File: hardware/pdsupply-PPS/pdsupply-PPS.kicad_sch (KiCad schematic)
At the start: 73 parts, among them IC1 LTM8083EY#PBF, IC2 FPF2895UCX, J1 USB4505-03-0-A_REVA, J2 USB4505-03-0-A_REVA, J3 Screw_Terminal_01x02, U1 FUSB307BMPX, U2 ADUM3160, U3 ACS71240KEXBLT-050U5, U4 STM32L432KCUx

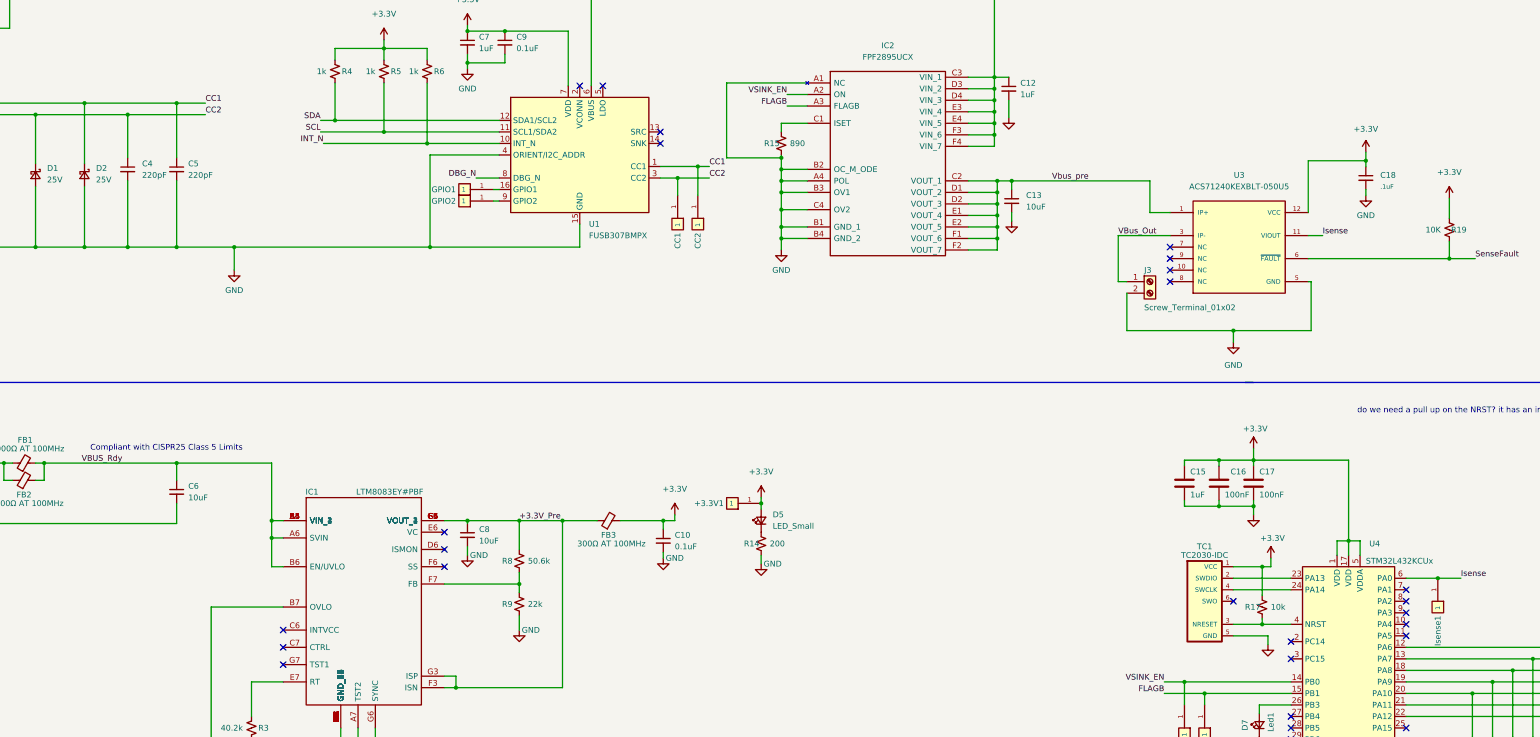
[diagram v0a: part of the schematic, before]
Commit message: changed Pin A1 on FPF2895 to be connected to GND
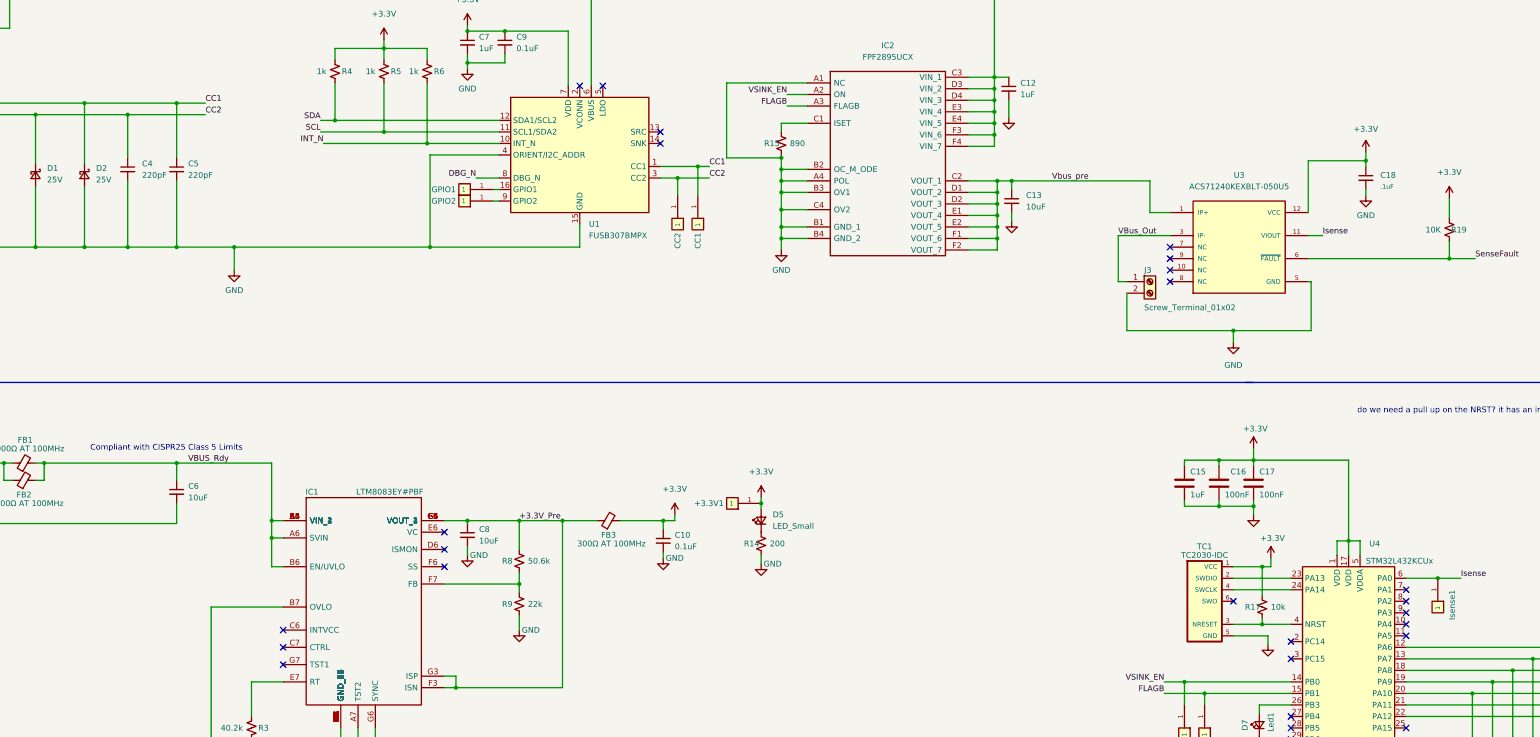
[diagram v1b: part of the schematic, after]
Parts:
- renumbered CC2 to CC1, CC1 to CC2
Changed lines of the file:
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@@
     (effects (font (size 1.27 1.27)) (justify left bottom))
   )
-  (label "VBUS_Rdy" (at 67.945 127 0)
+  (label "VBUS_Rdy" (at 91.44 127 0)
     (effects (font (size 1.27 1.27)) (justify left bottom))
   )
@@
   (symbol (lib_name "RCU-0C_1") (lib_id "RCU-0C:RCU-0C") (at 199.39 78.105 270) (unit 1)
     (in_bom yes) (on_board yes)
-    (property "Reference" "CC1" (id 0) (at 199.39 76.2 0)
+    (property "Reference" "CC2" (id 0) (at 199.39 76.2 0)
       (effects (font (size 1.27 1.27)) (justify left))
     )
@@
   (symbol (lib_name "RCU-0C_1") (lib_id "RCU-0C:RCU-0C") (at 203.835 78.105 270) (unit 1)
     (in_bom yes) (on_board yes)
-    (property "Reference" "CC2" (id 0) (at 203.835 76.2 0)
+    (property "Reference" "CC1" (id 0) (at 203.835 76.2 0)
       (effects (font (size 1.27 1.27)) (justify left))
     )
@@
   (symbol (lib_name "RCU-0C_1") (lib_id "RCU-0C:RCU-0C") (at 367.03 162.56 270) (unit 1)
     (in_bom yes) (on_board yes)
-    (property "Reference" "Isense1" (id 0) (at 367.03 160.655 0)
+    (property "Reference" "Isense1" (id 0) (at 370.205 154.94 0)
       (effects (font (size 1.27 1.27)) (justify left))
     )
@@
       (reference "C18") (unit 1) (value ".1uF") (footprint "Capacitor_SMD:C_0603_1608Metric")
     )
+    (path "/8aae3a86-de62-4041-9db6-c32f65e87d6d"
+      (reference "CC1") (unit 1) (value "RCU-0C") (footprint "RCU-0C:TP+195X110")
+    )
     (path "/28ec1f29-4986-4a9a-a39a-5d540d191da2"
-      (reference "CC1") (unit 1) (value "RCU-0C") (footprint "RCU-0C:TP+195X110")
-    )
-    (path "/8aae3a86-de62-4041-9db6-c32f65e87d6d"
       (reference "CC2") (unit 1) (value "RCU-0C") (footprint "RCU-0C:TP+195X110")
     )

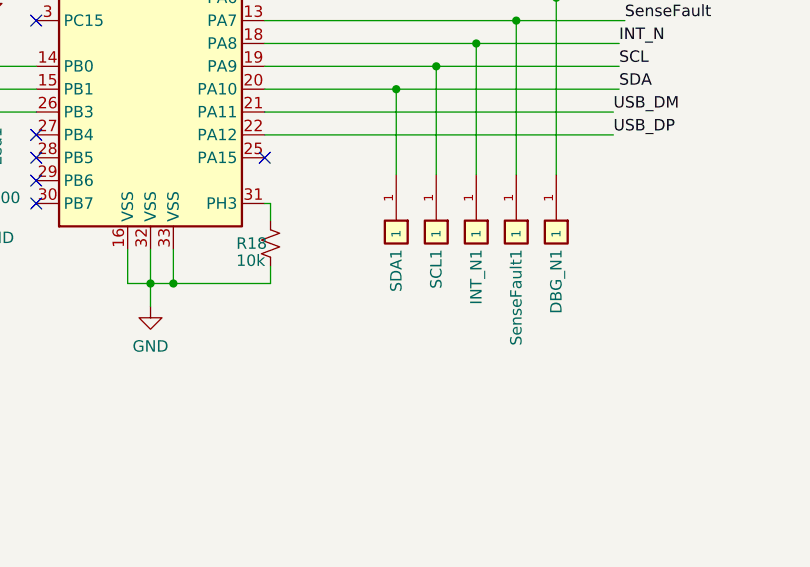
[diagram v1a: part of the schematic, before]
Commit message: fixed DRC violations
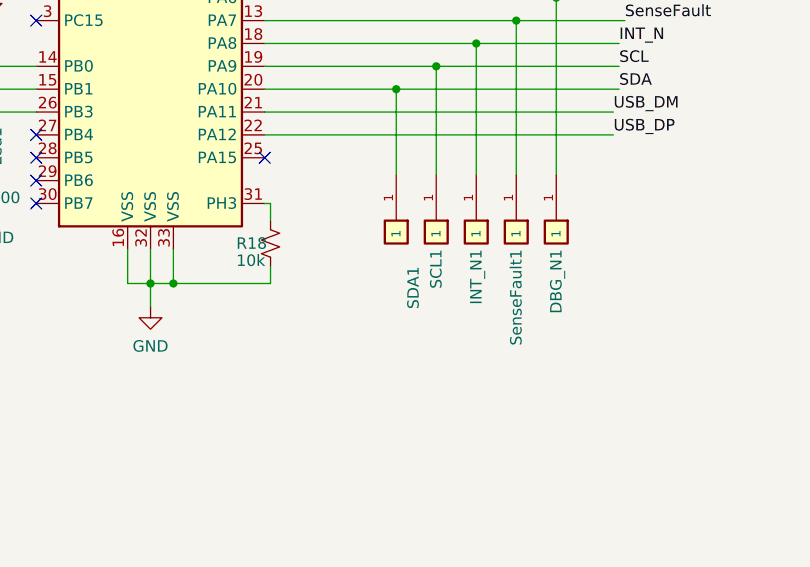
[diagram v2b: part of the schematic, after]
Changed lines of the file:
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@@
     (pin "1")
   )
-  (symbol (lib_name "RCU-0C_1") (lib_id "RCU-0C:RCU-0C") (at 374.65 197.485 270) (unit 1)
+  (symbol (lib_name "RCU-0C_2") (lib_id "RCU-0C:RCU-0C") (at 374.65 197.485 270) (unit 1)
     (in_bom yes) (on_board yes)
-    (property "Reference" "SDA1" (id 0) (at 374.65 195.58 0)
+    (property "Reference" "SDA1" (id 0) (at 376.555 197.485 0)
       (effects (font (size 1.27 1.27)) (justify left))
     )
-    (property "Value" "RCU-0C" (id 1) (at 370.84 193.04 0)
+    (property "Value" "RCU-0C" (id 1) (at 379.095 193.675 0)
       (effects (font (size 1.27 1.27)) (justify left) hide)
     )
